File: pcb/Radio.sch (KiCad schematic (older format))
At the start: 1 part

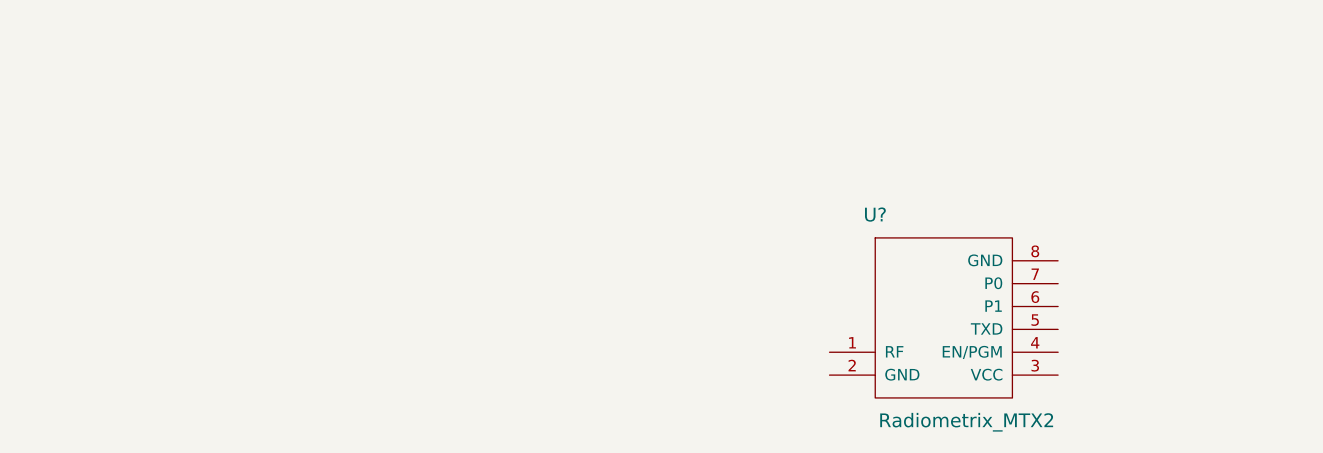
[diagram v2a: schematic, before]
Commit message: Add MTX2 circuit and add a sheet for power supply/regulation
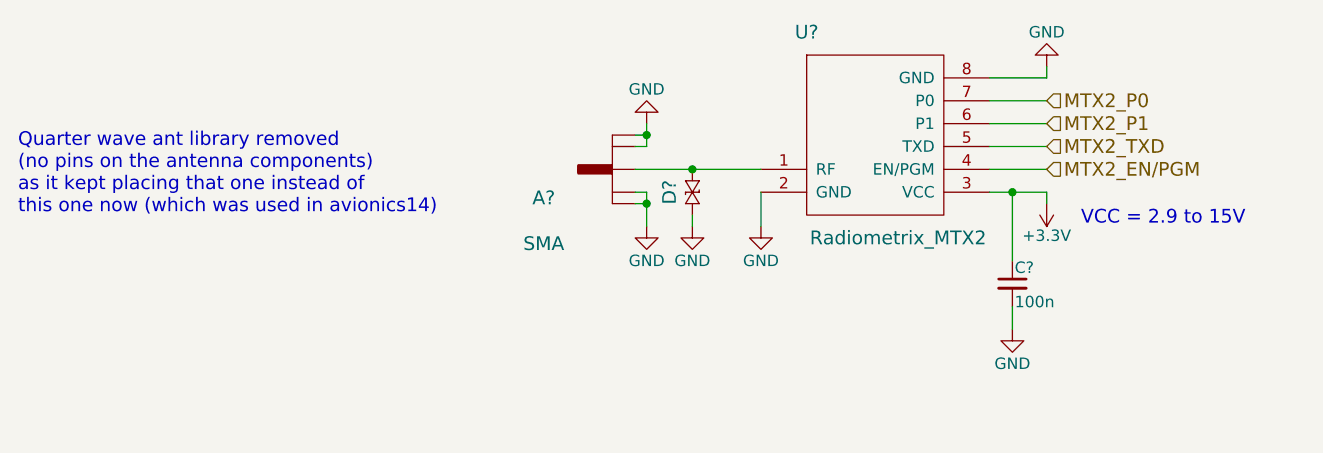
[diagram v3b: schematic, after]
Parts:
- added A?: SMA, Woodchuck:SMA-142-0701-801, symbol SMA
- added C?: 100n, Woodchuck:C0603, symbol C_Small
- added D?: CGA0402MLC-12G, Woodchuck:R0402, symbol CGA0402MLC-12G
- U?: Digikey (none) -> Value; Farnell (none) -> Value; Fieldname (none) -> Value
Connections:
- net at U?.1 (RF): now also A?.1 (RF), D?.1
- net GND: now reaches U?.2 (GND)
- net GND: now also U?.8 (GND), A?.2 (GND), A?.3 (GND), A?.4 (GND), A?.5 (GND), C?.2, D?.2
- net +3V3: now reaches U?.3 (VCC)
- net +3V3: now also C?.1
- net MTX2_EN/PGM: now reaches U?.4 (EN/PGM)
- net MTX2_TXD: now reaches U?.5 (TXD)
- net MTX2_P1: now reaches U?.6 (P1)
- net MTX2_P0: now reaches U?.7 (P0)
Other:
- note added: "Quarter wave ant library removed \n(no pins on the antenna components)\nas it kept placing that one instead of \nthis one now (which was used in avionics14)"
- note added: "VCC = 2.9 to 15V"
- moved on the sheet: U?
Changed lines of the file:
@@
 LIBS:max-7q
 LIBS:ms5611-01ba03
-LIBS:quarter_wave_ant
 LIBS:resistor
 LIBS:rfm69w
-LIBS:sma
 LIBS:stm32f405vgt
 LIBS:swd
@@
 LIBS:stm32f072cbt6
 LIBS:jsta
+LIBS:sma
+LIBS:cga0402mlc-12g
 LIBS:woodchuck-cache
 EELAYER 25 0
@@
 $Descr A4 11693 8268
 encoding utf-8
-Sheet 3 6
+Sheet 3 7
 Title ""
 Date ""
@@
 L Radiometrix_MTX2 U?
 U 1 1 5658C80F
-P 5850 3700
-F 0 "U?" H 5050 3900 60  0000 C CNN
-F 1 "Radiometrix_MTX2" H 5450 3000 60  0000 C CNN
-F 2 "" H 5850 3700 60  0000 C CNN
-F 3 "" H 5850 3700 60  0000 C CNN
-	1    5850 3700
-	1    0    0    -1
-$EndComp
+P 5550 2900
+F 0 "U?" H 4750 3100 60  0000 C CNN
+F 1 "Radiometrix_MTX2" H 5150 2200 60  0000 C CNN
+F 2 "" H 5550 2900 60  0000 C CNN
+F 3 "http://www.radiometrix.com/files/additional/mtx2.pdf" H 5550 2900 60  0001 C CNN
+F 4 "Value" H 5550 2900 60  0001 C CNN "Digikey"
+F 5 "Value" H 5550 2900 60  0001 C CNN "Farnell"
+F 6 "Value" H 5550 2900 60  0001 C CNN "Fieldname"
+	1    5550 2900
+	1    0    0    -1
+$EndComp
+$Comp
+L GND #PWR01
+U 1 1 565CEF3F
+P 5800 2850
+F 0 "#PWR01" H 5800 2600 50  0001 C CNN
+F 1 "GND" H 5800 2700 50  0000 C CNN
+F 2 "" H 5800 2850 60  0000 C CNN
+F 3 "" H 5800 2850 60  0000 C CNN
+	1    5800 2850
+	-1   0    0    1
+$EndComp
+$Comp
+L GND #PWR02
+U 1 1 565CEF57
+P 4550 3550
+F 0 "#PWR02" H 4550 3300 50  0001 C CNN
+F 1 "GND" H 4550 3400 50  0000 C CNN
+F 2 "" H 4550 3550 60  0000 C CNN
+F 3 "" H 4550 3550 60  0000 C CNN
+	1    4550 3550
+	1    0    0    -1
+$EndComp
+$Comp
+L SMA A?
+U 1 1 565CF9AA
+P 3900 3300
+F 0 "A?" H 4200 3425 60  0000 C CNN
+F 1 "SMA" H 4200 3625 60  0000 C CNN
+F 2 "Woodchuck:SMA-142-0701-801" H 4200 3625 60  0001 C CNN
+F 3 "" H 4200 3625 60  0000 C CNN
+F 4 "Value" H 3900 3300 60  0001 C CNN "Digikey"
+F 5 "1342651" H 3900 3300 60  0001 C CNN "Farnell"
+F 6 "Value" H 3900 3300 60  0001 C CNN "Fieldname"
+	1    3900 3300
+	-1   0    0    1
+$EndComp
+Text Notes 1300 3500 0    60   ~ 0
+Quarter wave ant library removed \n(no pins on the antenna components)\nas it kept placing that one instead of \nthis one now (which was used in avionics14)
+$Comp
+L GND #PWR?
+U 1 1 565D0220
+P 4050 3550
+F 0 "#PWR?" H 4050 3300 50  0001 C CNN
+F 1 "GND" H 4050 3400 50  0000 C CNN
+F 2 "" H 4050 3550 60  0000 C CNN
+F 3 "" H 4050 3550 60  0000 C CNN
+	1    4050 3550
+	1    0    0    -1
+$EndComp
+$Comp
+L GND #PWR?
+U 1 1 565D0231
+P 4050 3100
+F 0 "#PWR?" H 4050 2850 50  0001 C CNN
+F 1 "GND" H 4050 2950 50  0000 C CNN
+F 2 "" H 4050 3100 60  0000 C CNN
+F 3 "" H 4050 3100 60  0000 C CNN
+	1    4050 3100
+	-1   0    0    1
+$EndComp
+Wire Wire Line
+	4550 3400 4550 3550
+Wire Wire Line
+	4050 3100 4050 3200
+Wire Wire Line
+	4050 3200 4000 3200
+Wire Wire Line
+	4000 3150 4050 3150
+Connection ~ 4050 3150
+Wire Wire Line
+	4000 3400 4050 3400
+Wire Wire Line
+	4050 3400 4050 3550
+Wire Wire Line
+	4000 3450 4050 3450
+Connection ~ 4050 3450
+Text HLabel 5800 3000 2    60   Input ~ 0
+MTX2_P0
+Text HLabel 5800 3100 2    60   Input ~ 0
+MTX2_P1
+Text HLabel 5800 3200 2    60   Input ~ 0
+MTX2_TXD
+Text HLabel 5800 3300 2    60   Input ~ 0
+MTX2_EN/PGM
+$Comp
+L +3.3V #PWR?
+U 1 1 565D0F5D
+P 5800 3450
+F 0 "#PWR?" H 5800 3300 50  0001 C CNN
+F 1 "+3.3V" H 5800 3590 50  0000 C CNN
+F 2 "" H 5800 3450 60  0000 C CNN
+F 3 "" H 5800 3450 60  0000 C CNN
+	1    5800 3450
+	-1   0    0    1
+$EndComp
+Wire Wire Line
+	5800 2850 5800 2900
+Wire Wire Line
+	5800 2900 5550 2900
+Wire Wire Line
+	5550 3000 5800 3000
+Wire Wire Line
+	5550 3100 5800 3100
+Wire Wire Line
+	5550 3200 5800 3200
+Wire Wire Line
+	5550 3300 5800 3300
+Wire Wire Line
+	5800 3450 5800 3400
+Wire Wire Line
+	5800 3400 5550 3400
+Text Notes 5950 3550 0    60   ~ 0
+VCC = 2.9 to 15V
+$Comp
+L C_Small C?
+U 1 1 565D1347
+P 5650 3800
+F 0 "C?" H 5660 3870 50  0000 L CNN
+F 1 "100n" H 5660 3720 50  0000 L CNN
+F 2 "Woodchuck:C0603" H 5650 3800 60  0001 C CNN
+F 3 "" H 5650 3800 60  0000 C CNN
+F 4 "Value" H 5650 3800 60  0001 C CNN "Digikey"
+F 5 "1759037" H 5650 3800 60  0001 C CNN "Farnell"
+F 6 "Value" H 5650 3800 60  0001 C CNN "Fieldname"
+	1    5650 3800
+	1    0    0    -1
+$EndComp
+$Comp
+L GND #PWR?
+U 1 1 565D1392
+P 5650 4000
+F 0 "#PWR?" H 5650 3750 50  0001 C CNN
+F 1 "GND" H 5650 3850 50  0000 C CNN
+F 2 "" H 5650 4000 60  0000 C CNN
+F 3 "" H 5650 4000 60  0000 C CNN
+	1    5650 4000
+	1    0    0    -1
+$EndComp
+Wire Wire Line
+	5650 3700 5650 3400
+Connection ~ 5650 3400
+Wire Wire Line
+	5650 4000 5650 3900
+$Comp
+L CGA0402MLC-12G D?
+U 1 1 565D14D2
+P 4250 3300
+F 0 "D?" H 4350 3200 60  0000 C CNN
+F 1 "CGA0402MLC-12G" H 4350 3410 60  0001 C CNN
+F 2 "Woodchuck:R0402" H 4250 3300 60  0001 C BNN
+F 3 "" H 4250 3300 60  0000 C CNN
+F 4 "Value" H 4250 3300 60  0001 C CNN "Digikey"
+F 5 "2368169" H 4250 3300 60  0001 C CNN "Farnell"
+F 6 "Value" H 4250 3300 60  0001 C CNN "Fieldname"
+	1    4250 3300
+	0    1    1    0
+$EndComp
+$Comp
+L GND #PWR?
+U 1 1 565D162B
+P 4250 3550
+F 0 "#PWR?" H 4250 3300 50  0001 C CNN
+F 1 "GND" H 4250 3400 50  0000 C CNN
+F 2 "" H 4250 3550 60  0000 C CNN
+F 3 "" H 4250 3550 60  0000 C CNN
+	1    4250 3550
+	1    0    0    -1
+$EndComp
+Wire Wire Line
+	4250 3550 4250 3500
+Wire Wire Line
+	4000 3300 4550 3300
+Connection ~ 4250 3300
 $EndSCHEMATC

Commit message: Add MTX2 footprint library from m2r
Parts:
- A?: Farnell 1342651 -> 1608592
- U?: footprint (none) -> Woodchuck:MTX2
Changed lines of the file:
@@
 F 0 "U?" H 4750 3100 60  0000 C CNN
 F 1 "Radiometrix_MTX2" H 5150 2200 60  0000 C CNN
-F 2 "" H 5550 2900 60  0000 C CNN
+F 2 "Woodchuck:MTX2" H 5550 2900 60  0001 C CNN
 F 3 "http://www.radiometrix.com/files/additional/mtx2.pdf" H 5550 2900 60  0001 C CNN
 F 4 "Value" H 5550 2900 60  0001 C CNN "Digikey"
@@
 F 3 "" H 4200 3625 60  0000 C CNN
 F 4 "Value" H 3900 3300 60  0001 C CNN "Digikey"
-F 5 "1342651" H 3900 3300 60  0001 C CNN "Farnell"
+F 5 "1608592" H 3900 3300 60  0001 C CNN "Farnell"
 F 6 "Value" H 3900 3300 60  0001 C CNN "Fieldname"
 	1    3900 3300

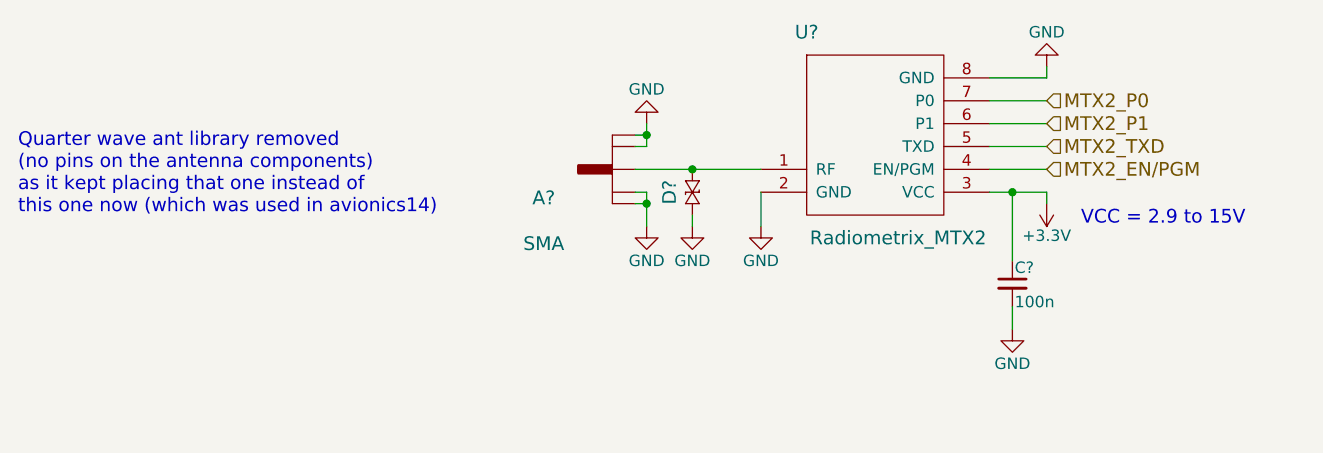
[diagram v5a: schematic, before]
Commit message: Modify pin assignments of MCU
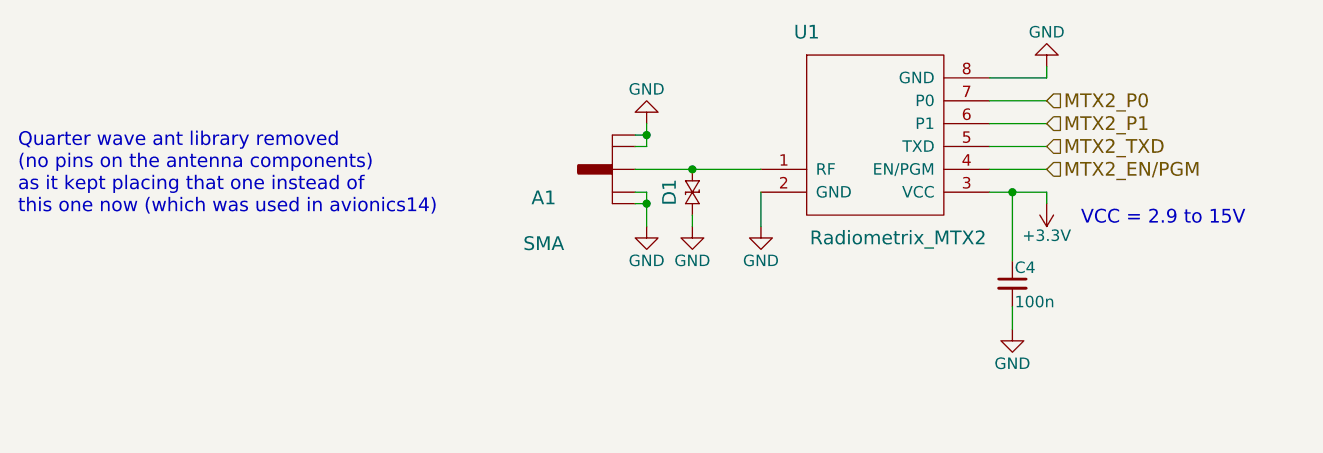
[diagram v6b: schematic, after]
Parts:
- gave numbers to parts that had none: 4
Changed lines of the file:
@@
 $EndDescr
 $Comp
-L Radiometrix_MTX2 U?
+L Radiometrix_MTX2 U1
 U 1 1 5658C80F
 P 5550 2900
-F 0 "U?" H 4750 3100 60  0000 C CNN
+F 0 "U1" H 4750 3100 60  0000 C CNN
 F 1 "Radiometrix_MTX2" H 5150 2200 60  0000 C CNN
 F 2 "Woodchuck:MTX2" H 5550 2900 60  0001 C CNN
@@
 $EndComp
 $Comp
-L GND #PWR01
+L GND #PWR05
 U 1 1 565CEF3F
 P 5800 2850
-F 0 "#PWR01" H 5800 2600 50  0001 C CNN
+F 0 "#PWR05" H 5800 2600 50  0001 C CNN
 F 1 "GND" H 5800 2700 50  0000 C CNN
 F 2 "" H 5800 2850 60  0000 C CNN
@@
 $EndComp
 $Comp
-L GND #PWR02
+L GND #PWR06
 U 1 1 565CEF57
 P 4550 3550
-F 0 "#PWR02" H 4550 3300 50  0001 C CNN
+F 0 "#PWR06" H 4550 3300 50  0001 C CNN
 F 1 "GND" H 4550 3400 50  0000 C CNN
 F 2 "" H 4550 3550 60  0000 C CNN
@@
 $EndComp
 $Comp
-L SMA A?
+L SMA A1
 U 1 1 565CF9AA
 P 3900 3300
-F 0 "A?" H 4200 3425 60  0000 C CNN
+F 0 "A1" H 4200 3425 60  0000 C CNN
 F 1 "SMA" H 4200 3625 60  0000 C CNN
 F 2 "Woodchuck:SMA-142-0701-801" H 4200 3625 60  0001 C CNN
@@
 Quarter wave ant library removed \n(no pins on the antenna components)\nas it kept placing that one instead of \nthis one now (which was used in avionics14)
 $Comp
-L GND #PWR?
+L GND #PWR07
 U 1 1 565D0220
 P 4050 3550
-F 0 "#PWR?" H 4050 3300 50  0001 C CNN
+F 0 "#PWR07" H 4050 3300 50  0001 C CNN
 F 1 "GND" H 4050 3400 50  0000 C CNN
 F 2 "" H 4050 3550 60  0000 C CNN
@@
 $EndComp
 $Comp
-L GND #PWR?
+L GND #PWR08
 U 1 1 565D0231
 P 4050 3100
-F 0 "#PWR?" H 4050 2850 50  0001 C CNN
+F 0 "#PWR08" H 4050 2850 50  0001 C CNN
 F 1 "GND" H 4050 2950 50  0000 C CNN
 F 2 "" H 4050 3100 60  0000 C CNN
@@
 MTX2_EN/PGM
 $Comp
-L +3.3V #PWR?
+L +3.3V #PWR09
 U 1 1 565D0F5D
 P 5800 3450
-F 0 "#PWR?" H 5800 3300 50  0001 C CNN
+F 0 "#PWR09" H 5800 3300 50  0001 C CNN
 F 1 "+3.3V" H 5800 3590 50  0000 C CNN
 F 2 "" H 5800 3450 60  0000 C CNN
@@
 VCC = 2.9 to 15V
 $Comp
-L C_Small C?
+L C_Small C4
 U 1 1 565D1347
 P 5650 3800
-F 0 "C?" H 5660 3870 50  0000 L CNN
+F 0 "C4" H 5660 3870 50  0000 L CNN
 F 1 "100n" H 5660 3720 50  0000 L CNN
 F 2 "Woodchuck:C0603" H 5650 3800 60  0001 C CNN
@@
 $EndComp
 $Comp
-L GND #PWR?
+L GND #PWR010
 U 1 1 565D1392
 P 5650 4000
-F 0 "#PWR?" H 5650 3750 50  0001 C CNN
+F 0 "#PWR010" H 5650 3750 50  0001 C CNN
 F 1 "GND" H 5650 3850 50  0000 C CNN
 F 2 "" H 5650 4000 60  0000 C CNN
@@
 	5650 4000 5650 3900
 $Comp
-L CGA0402MLC-12G D?
+L CGA0402MLC-12G D1
 U 1 1 565D14D2
 P 4250 3300
-F 0 "D?" H 4350 3200 60  0000 C CNN
+F 0 "D1" H 4350 3200 60  0000 C CNN
 F 1 "CGA0402MLC-12G" H 4350 3410 60  0001 C CNN
 F 2 "Woodchuck:R0402" H 4250 3300 60  0001 C BNN
@@
 $EndComp
 $Comp
-L GND #PWR?
+L GND #PWR011
 U 1 1 565D162B
 P 4250 3550
-F 0 "#PWR?" H 4250 3300 50  0001 C CNN
+F 0 "#PWR011" H 4250 3300 50  0001 C CNN
 F 1 "GND" H 4250 3400 50  0000 C CNN
 F 2 "" H 4250 3550 60  0000 C CNN

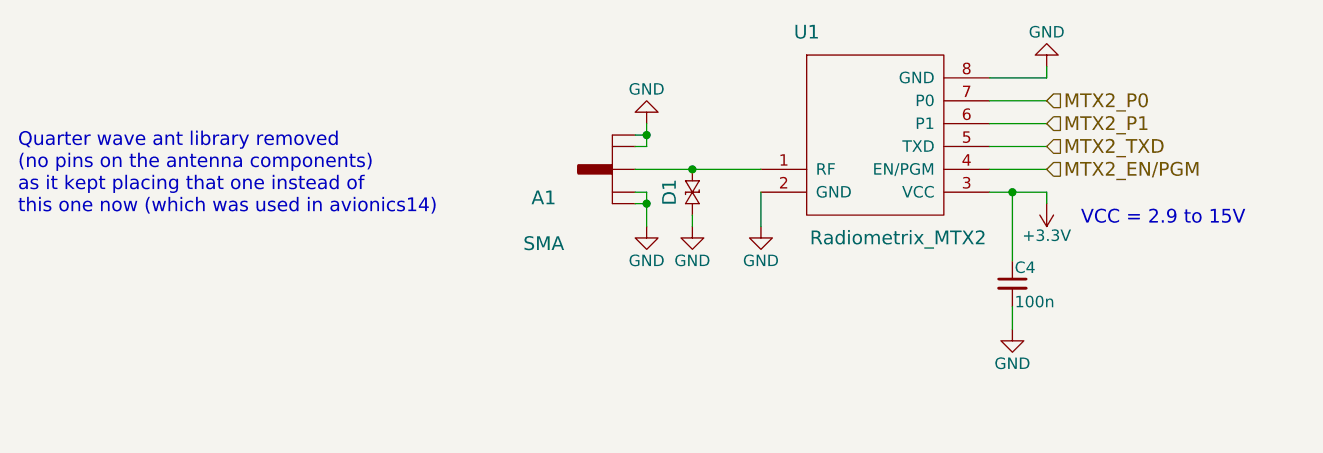
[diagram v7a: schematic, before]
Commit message: Generated net list (only two footprints remaining), added a few footprints, started rough estimate of PCB size
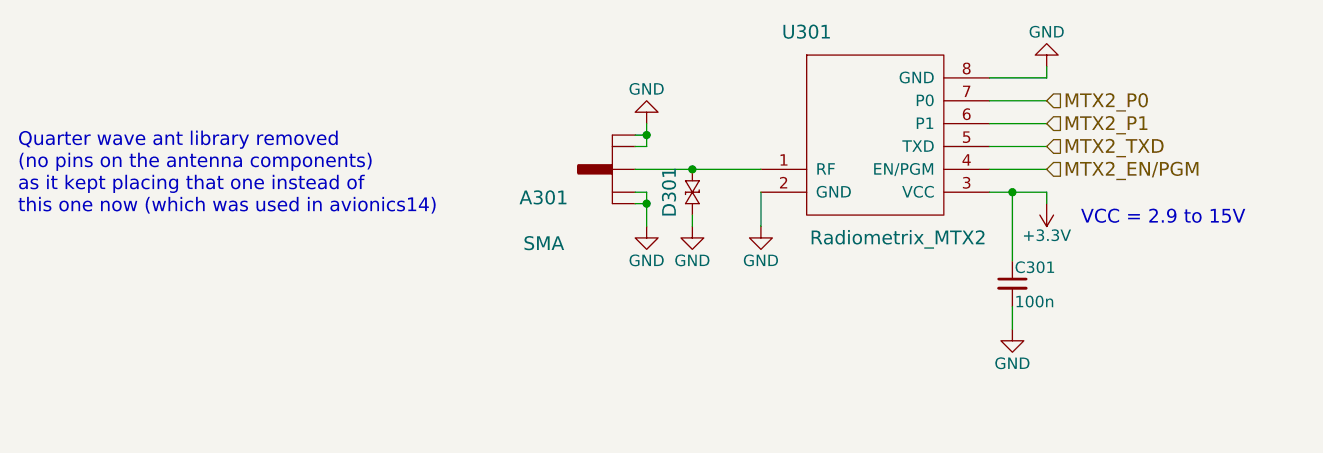
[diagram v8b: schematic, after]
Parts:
- renumbered A1 to A301, C4 to C301, D1 to D301, U1 to U301
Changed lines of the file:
@@
 $EndDescr
 $Comp
-L Radiometrix_MTX2 U1
+L Radiometrix_MTX2 U301
 U 1 1 5658C80F
 P 5550 2900
-F 0 "U1" H 4750 3100 60  0000 C CNN
+F 0 "U301" H 4750 3100 60  0000 C CNN
 F 1 "Radiometrix_MTX2" H 5150 2200 60  0000 C CNN
 F 2 "Woodchuck:MTX2" H 5550 2900 60  0001 C CNN
@@
 $EndComp
 $Comp
-L GND #PWR10
+L GND #PWR010
 U 1 1 565CEF3F
 P 5800 2850
-F 0 "#PWR10" H 5800 2600 50  0001 C CNN
+F 0 "#PWR010" H 5800 2600 50  0001 C CNN
 F 1 "GND" H 5800 2700 50  0000 C CNN
 F 2 "" H 5800 2850 60  0000 C CNN
@@
 $EndComp
 $Comp
-L GND #PWR8
+L GND #PWR011
 U 1 1 565CEF57
 P 4550 3550
-F 0 "#PWR8" H 4550 3300 50  0001 C CNN
+F 0 "#PWR011" H 4550 3300 50  0001 C CNN
 F 1 "GND" H 4550 3400 50  0000 C CNN
 F 2 "" H 4550 3550 60  0000 C CNN
@@
 $EndComp
 $Comp
-L SMA A1
+L SMA A301
 U 1 1 565CF9AA
 P 3900 3300
-F 0 "A1" H 4200 3425 60  0000 C CNN
+F 0 "A301" H 4200 3425 60  0000 C CNN
 F 1 "SMA" H 4200 3625 60  0000 C CNN
 F 2 "Woodchuck:SMA-142-0701-801" H 4200 3625 60  0001 C CNN
@@
 Quarter wave ant library removed \n(no pins on the antenna components)\nas it kept placing that one instead of \nthis one now (which was used in avionics14)
 $Comp
-L GND #PWR6
+L GND #PWR012
 U 1 1 565D0220
 P 4050 3550
-F 0 "#PWR6" H 4050 3300 50  0001 C CNN
+F 0 "#PWR012" H 4050 3300 50  0001 C CNN
 F 1 "GND" H 4050 3400 50  0000 C CNN
 F 2 "" H 4050 3550 60  0000 C CNN
@@
 $EndComp
 $Comp
-L GND #PWR5
+L GND #PWR013
 U 1 1 565D0231
 P 4050 3100
-F 0 "#PWR5" H 4050 2850 50  0001 C CNN
+F 0 "#PWR013" H 4050 2850 50  0001 C CNN
 F 1 "GND" H 4050 2950 50  0000 C CNN
 F 2 "" H 4050 3100 60  0000 C CNN
@@
 MTX2_EN/PGM
 $Comp
-L +3.3V #PWR11
+L +3.3V #PWR014
 U 1 1 565D0F5D
 P 5800 3450
-F 0 "#PWR11" H 5800 3300 50  0001 C CNN
+F 0 "#PWR014" H 5800 3300 50  0001 C CNN
 F 1 "+3.3V" H 5800 3590 50  0000 C CNN
 F 2 "" H 5800 3450 60  0000 C CNN
@@
 VCC = 2.9 to 15V
 $Comp
-L C_Small C4
+L C_Small C301
 U 1 1 565D1347
 P 5650 3800
-F 0 "C4" H 5660 3870 50  0000 L CNN
+F 0 "C301" H 5660 3870 50  0000 L CNN
 F 1 "100n" H 5660 3720 50  0000 L CNN
 F 2 "Woodchuck:C0603" H 5650 3800 60  0001 C CNN
@@
 $EndComp
 $Comp
-L GND #PWR9
+L GND #PWR015
 U 1 1 565D1392
 P 5650 4000
-F 0 "#PWR9" H 5650 3750 50  0001 C CNN
+F 0 "#PWR015" H 5650 3750 50  0001 C CNN
 F 1 "GND" H 5650 3850 50  0000 C CNN
 F 2 "" H 5650 4000 60  0000 C CNN
@@
 	5650 4000 5650 3900
 $Comp
-L CGA0402MLC-12G D1
+L CGA0402MLC-12G D301
 U 1 1 565D14D2
 P 4250 3300
-F 0 "D1" H 4350 3200 60  0000 C CNN
+F 0 "D301" H 4350 3200 60  0000 C CNN
 F 1 "CGA0402MLC-12G" H 4350 3410 60  0001 C CNN
 F 2 "Woodchuck:R0402" H 4250 3300 60  0001 C BNN
@@
 $EndComp
 $Comp
-L GND #PWR7
+L GND #PWR016
 U 1 1 565D162B
 P 4250 3550
-F 0 "#PWR7" H 4250 3300 50  0001 C CNN
+F 0 "#PWR016" H 4250 3300 50  0001 C CNN
 F 1 "GND" H 4250 3400 50  0000 C CNN
 F 2 "" H 4250 3550 60  0000 C CNN
